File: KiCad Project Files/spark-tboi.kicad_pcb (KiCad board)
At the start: 4 copper layers, 155.4 x 101.8 mm, 39 parts, among them IC1 STM32F103C8T7, X1 Y32258MNCCZ

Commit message: added case
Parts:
- added REF**: MountingHole_2.2mm_M2, MountingHole:MountingHole_2.2mm_M2, F.Cu at (177.0, 100.0)
- added REF**: MountingHole_2.2mm_M2, MountingHole:MountingHole_2.2mm_M2, F.Cu at (32.0, 120.0)
- added REF**: MountingHole_2.2mm_M2, MountingHole:MountingHole_2.2mm_M2, F.Cu at (31.5, 27.5)
- added REF**: MountingHole_2.2mm_M2, MountingHole:MountingHole_2.2mm_M2, F.Cu at (176.5, 29.0)
- added REF**: MountingHole_2.2mm_M2, MountingHole:MountingHole_2.2mm_M2, F.Cu at (105.0, 117.0)

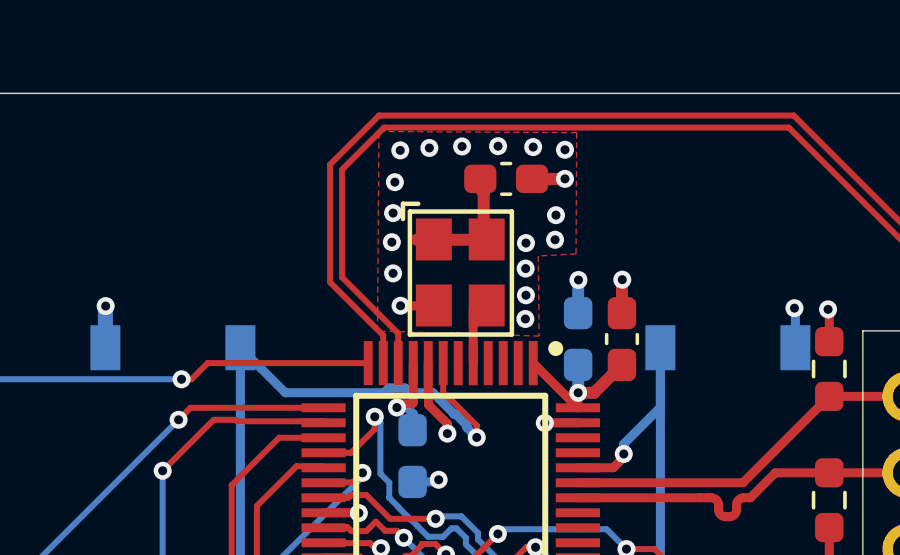
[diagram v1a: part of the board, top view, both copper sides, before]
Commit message: Changed distributor to TME
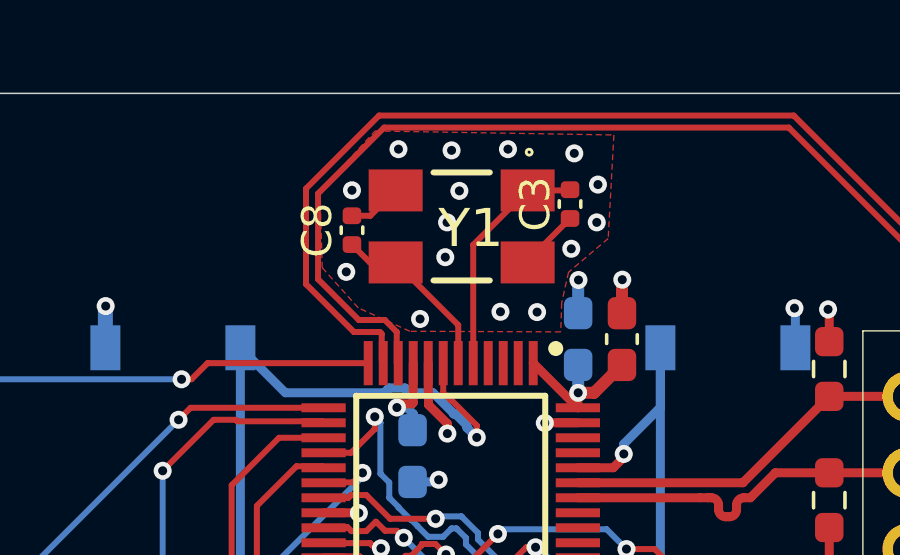
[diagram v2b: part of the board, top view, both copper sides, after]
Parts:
- removed X1: Y32258MNCCZ, easyeda2kicad:OSC-SMD_4P-L3.2-W2.5-BL
- added C8: 18pF, REQ:C_0402_1005Metric, F.Cu at (97.5, 27.6)
- added Y1: ABMM2-8.000MHZ-E2-T, REQ:ABMM2, F.Cu at (101.1, 27.5)
- 3V3_LDO1: footprint easyeda2kicad:SOT-223-3_L6.7-W3.7-P2.30-LS7.0-BR -> REQ:SOT-223-3_L6.7-W3.7-P2.30-LS7.0-BR
- BOOT_BUTTON1, NRST_BUTTON1: footprint easyeda2kicad:SW-SMD_4P-L6.2-W6.0-P4.50-LS9.0 -> REQ:SW-SMD_4P-L6.2-W6.0-P4.50-LS9.0
- C1, C2, C4, C5, C6, C7: footprint Capacitor_SMD:C_0603_1608Metric_Pad1.08x0.95mm_HandSolder -> REQ:C_0603_1608Metric_Pad1.08x0.95mm_HandSolder
- C3: value 100nF -> 18pF; footprint Capacitor_SMD:C_0603_1608Metric_Pad1.08x0.95mm_HandSolder -> REQ:C_0402_1005Metric
- CC_TVS1, DATA_TVS1: footprint easyeda2kicad:SC-75-3_L1.6-W0.8-P1.00-LS1.6-BR -> REQ:SC-75-3_L1.6-W0.8-P1.00-LS1.6-BR
- CH1, CH10, CH11, CH12, CH13, CH14, CH15, CH2, CH3, CH4, CH5, CH6, CH7, CH8, CH9: footprint PCM_marbastlib-mx:SW_MX_HS_CPG151101S11_1u -> REQ:SW_MX_HS_CPG151101S11_1u
- ENCODER1: footprint ec11:RotaryEncoder_Alps_EC11E_Vertical_H20mm -> REQ:RotaryEncoder_Alps_EC11E_Vertical_H20mm
- IC1: footprint STM32F103C8T7:QFP50P900X900X160-48N -> REQ:QFP50P900X900X160-48N
- OLED1: footprint oled:SSD1306-0.91-OLED-4pin-128x32 -> REQ:SSD1306-0.91-OLED-4pin-128x32
- R1, R2, R3, R4: footprint Resistor_SMD:R_0603_1608Metric_Pad0.98x0.95mm_HandSolder -> REQ:R_0603_1608Metric_Pad0.98x0.95mm_HandSolder
- R5: value 4.7kOhm -> 5.1kOhm; footprint Resistor_SMD:R_0603_1608Metric_Pad0.98x0.95mm_HandSolder -> REQ:R_0603_1608Metric_Pad0.98x0.95mm_HandSolder
- REF** (x5): footprint MountingHole:MountingHole_2.2mm_M2 -> REQ:MountingHole_2.2mm_M2
- UART1: footprint Connector_Wire:SolderWire-0.1sqmm_1x03_P3.6mm_D0.4mm_OD1mm -> REQ:SolderWire-0.1sqmm_1x03_P3.6mm_D0.4mm_OD1mm
- USB1: footprint easyeda2kicad:USB-C-SMD_TYPE-C-6PIN-2MD-073 -> REQ:USB-C-SMD_TYPE-C-6PIN-2MD-073
- VBUS_TVS1: footprint easyeda2kicad:SMB_L4.6-W3.6-LS5.3-RD -> REQ:SMB_L4.6-W3.6-LS5.3-RD
- moved C3 2.29 mm to (104.7, 26.7), turned to 90 degrees
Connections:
- C3 pad 1: +3.3V -> GND
- C3 pad 2: GND -> Net-(IC1-PD0-OSC_IN)
- ENCODER1 pad : GND -> (no net)
- IC1 pad 6: unconnected-(IC1-PD1-OSC_OUT-Pad6) -> Net-(IC1-PD1-OSC_OUT)
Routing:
- net Net-(IC1-PD1-OSC_OUT): track 0.00 -> 5.92 mm
- net Net-(IC1-PD0-OSC_IN): track 2.29 -> 7.93 mm
- net +3.3V: track 21.5 -> 17.0 mm
- net GND: track 30.5 -> 32.4 mm, vias 40 -> 37
- net ROTARY_A: track 77.2 -> 78.4 mm
- net ROTARY_B: track 80.2 -> 81.3 mm
